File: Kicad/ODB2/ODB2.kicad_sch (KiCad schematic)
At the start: 32 parts, among them U1 STM32F412ZGTx

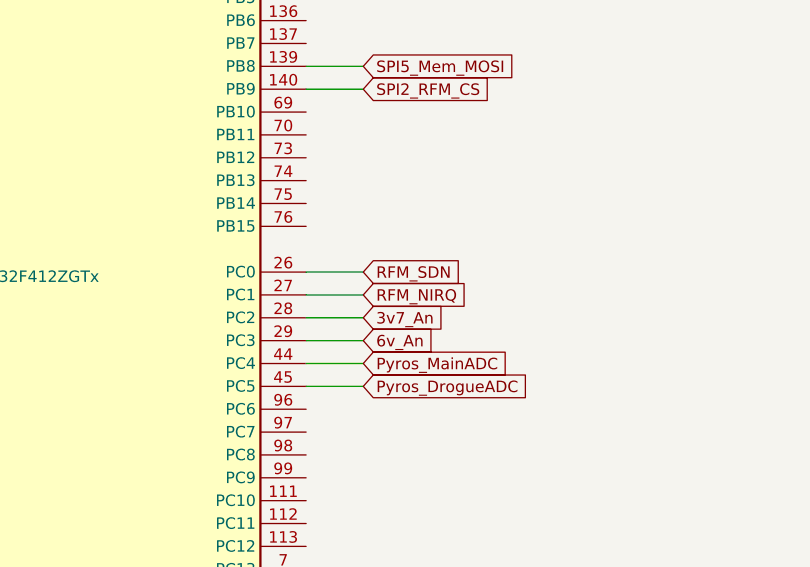
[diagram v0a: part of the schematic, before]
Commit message: Changed label 6v to 6v6 and changed circuit for the 6v6 batt led
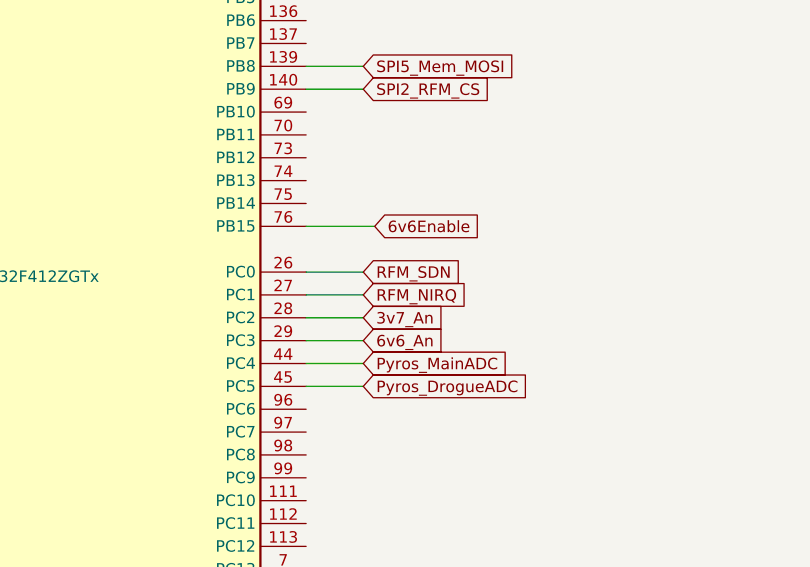
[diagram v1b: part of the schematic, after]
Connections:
- net 6v6Enable: now reaches U1.76 (PB15)
- net 6v_An renamed 6v6_An
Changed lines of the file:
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@@
+	(wire
+		(pts
+			(xy 231.14 137.16) (xy 238.76 137.16)
+		)
+		(stroke
+			(width 0)
+			(type default)
+		)
+	)
 	(wire
 		(pts
@@
 		)
 	)
+	(global_label "6v6Enable"
+		(shape input)
+		(at 238.76 137.16 0)
+		(fields_autoplaced yes)
+		(effects
+			(font
+				(size 1.27 1.27)
+			)
+			(justify left)
+		)
+		(property "Intersheetrefs" "${INTERSHEET_REFS}"
+			(at 251.4816 137.16 0)
+			(effects
+				(font
+					(size 1.27 1.27)
+				)
+				(justify left)
+				(hide yes)
+			)
+		)
+	)
 	(global_label "SPI5_Mem_MISO"
 		(shape input)
@@
 		)
 	)
-	(global_label "6v_An"
+	(global_label "6v6_An"
 		(shape input)
 		(at 237.49 149.86 0)
@@
 		)
 		(property "Intersheetrefs" "${INTERSHEET_REFS}"
-			(at 245.8575 149.86 0)
-			(effects
-				(font
+			(at 247.067 149.86 0)
+			(effects
+				(font

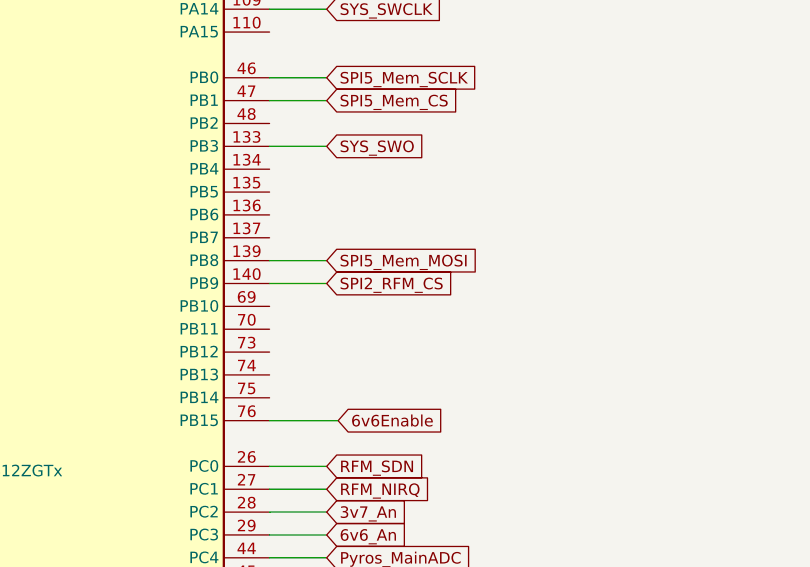
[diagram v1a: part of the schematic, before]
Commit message: fix spi label
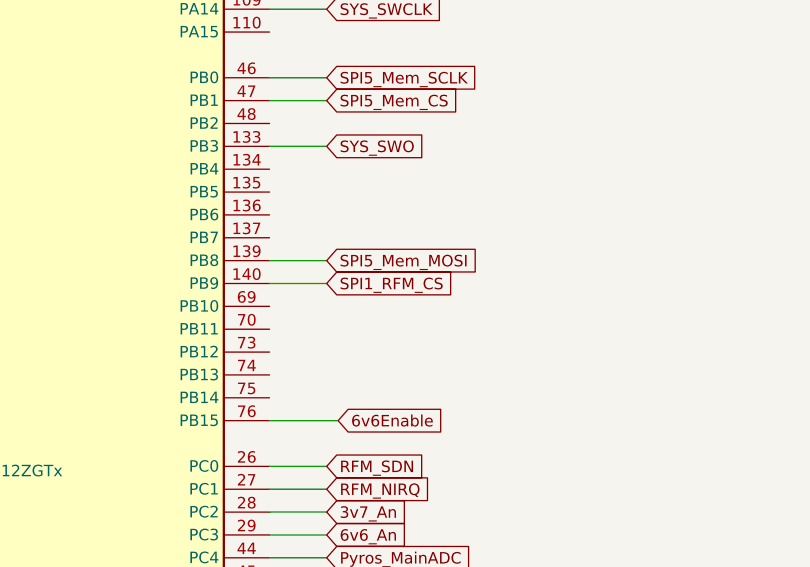
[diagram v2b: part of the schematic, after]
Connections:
- net SPI2_RFM_CS renamed SPI1_RFM_CS
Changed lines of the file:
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@@
 		)
 	)
-	(global_label "SPI2_RFM_CS"
+	(global_label "SPI1_RFM_CS"
 		(shape input)
 		(at 237.49 121.92 0)

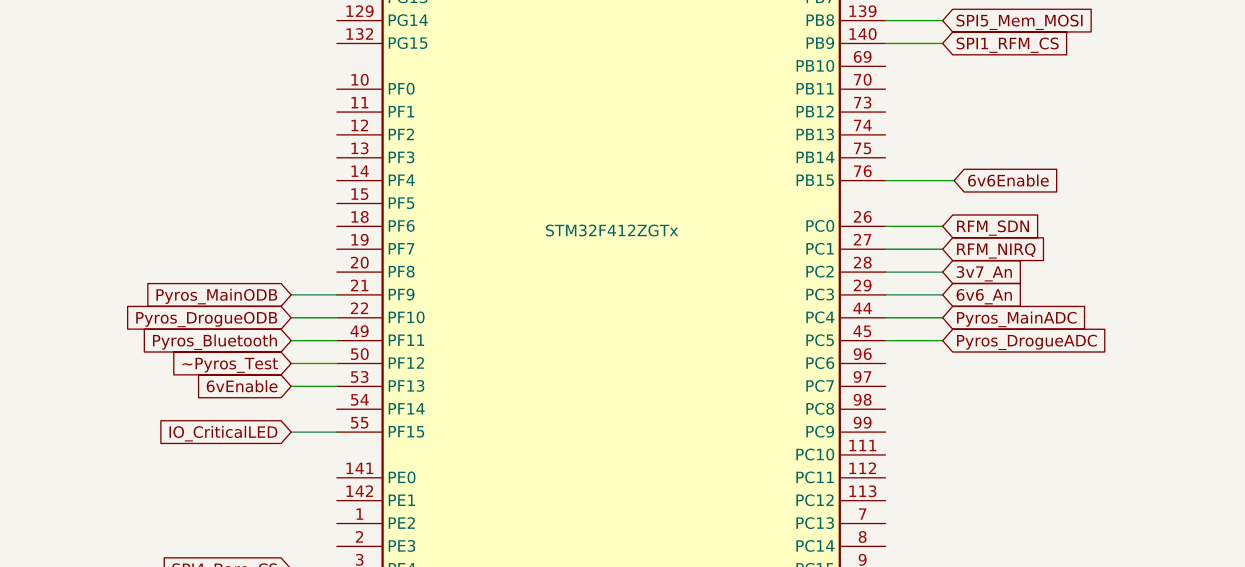
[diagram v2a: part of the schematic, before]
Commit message: fix 6v6Enable label
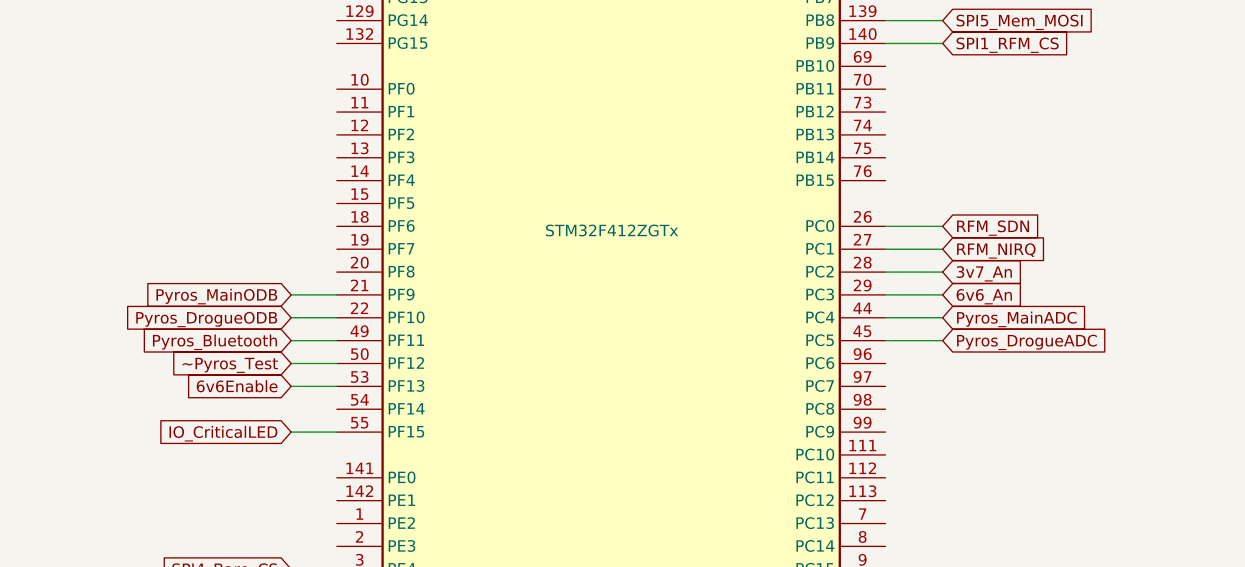
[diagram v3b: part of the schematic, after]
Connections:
- net 6vEnable is gone; now on net 6v6Enable: U1.53 (PF13)
- net 6v6Enable: no longer U1.76 (PB15)
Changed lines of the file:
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@@
-	(wire
-		(pts
-			(xy 231.14 137.16) (xy 238.76 137.16)
-		)
-		(stroke
-			(width 0)
-			(type default)
-		)
-	)
 	(wire
 		(pts
@@
 		)
 	)
-	(global_label "6vEnable"
+	(global_label "6v6Enable"
 		(shape input)
 		(at 165.1 160.02 180)
@@
 		)
 		(property "Intersheetrefs" "${INTERSHEET_REFS}"
-			(at 153.5879 160.02 0)
+			(at 152.3784 160.02 0)
 			(effects
 				(font
@@
 				(hide yes)
 			)
-		)
-	)
-	(global_label "6v6Enable"
-		(shape input)
-		(at 238.76 137.16 0)
-		(fields_autoplaced yes)
-		(effects
-			(font
-				(size 1.27 1.27)
-			)
-			(justify left)
-		)
-		(property "Intersheetrefs" "${INTERSHEET_REFS}"
-			(at 251.4816 137.16 0)
-			(effects
-				(font
-					(size 1.27 1.27)
-				)
-				(justify left)
-				(hide yes)
-			)

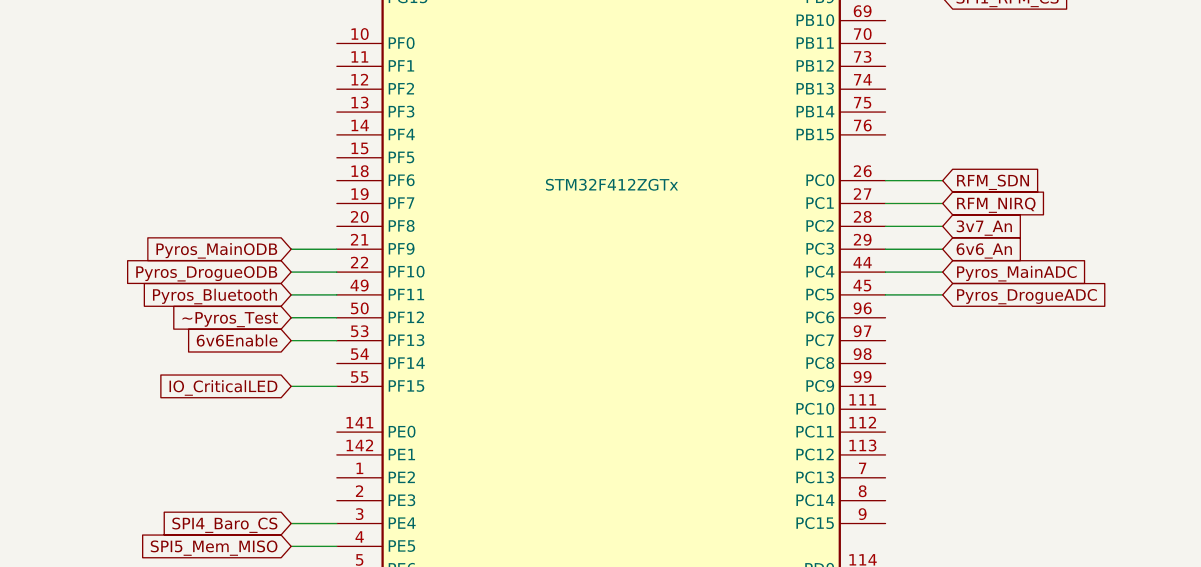
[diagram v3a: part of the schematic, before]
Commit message: changer LiFePO4 pour LiPo
recalculer le bon ration pour l'ADC du 4v2 input (anciennement 3v7 input) et modifier ces labels associées

modifier le bon ration (je crois) pour l'ADC du 7v4 isolation (anciennement 6v isolation) et modifier ces labels associées
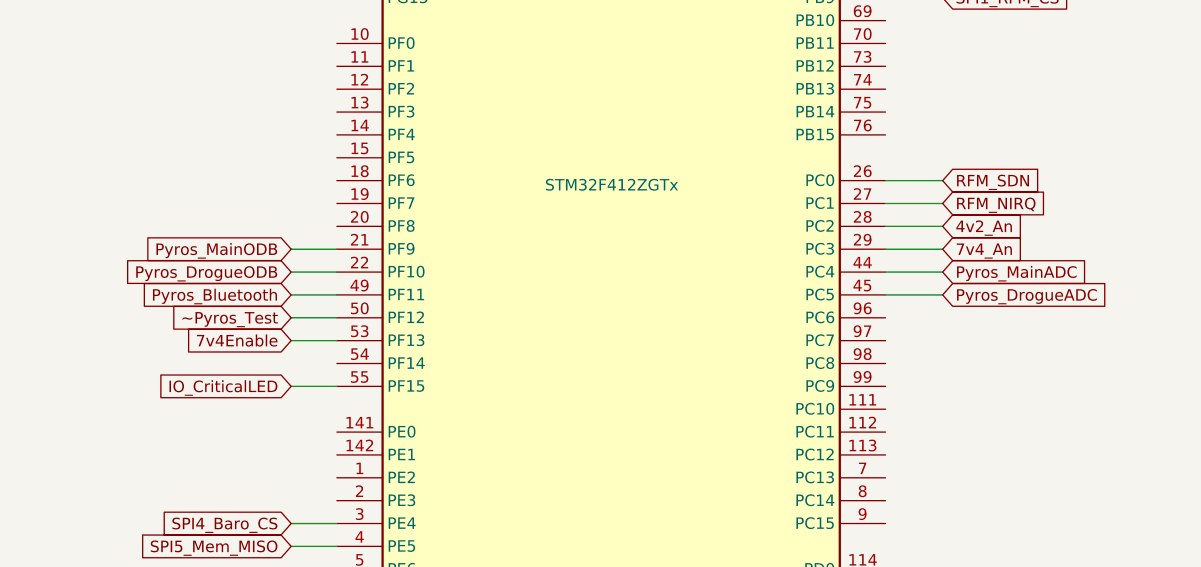
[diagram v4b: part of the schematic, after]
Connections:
- net 3v7_An renamed 4v2_An
- net 6v6Enable renamed 7v4Enable
- net 6v6_An renamed 7v4_An
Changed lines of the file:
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@@
 		)
 	)
-	(global_label "6v6Enable"
+	(global_label "7v4Enable"
 		(shape input)
 		(at 165.1 160.02 180)
@@
 		)
 	)
+	(global_label "4v2_An"
+		(shape input)
+		(at 237.49 147.32 0)
+		(fields_autoplaced yes)
+		(effects
+			(font
+				(size 1.27 1.27)
+			)
+			(justify left)
+		)
+		(property "Intersheetrefs" "${INTERSHEET_REFS}"
+			(at 247.067 147.32 0)
+			(effects
+				(font
+					(size 1.27 1.27)
+				)
+				(justify left)
+				(hide yes)
+			)
+		)
+	)
 	(global_label "SPI1_ICM_RFM_MOSI"
 		(shape input)
@@
 		)
 	)
-	(global_label "3v7_An"
-		(shape input)
-		(at 237.49 147.32 0)
-		(fields_autoplaced yes)
-		(effects
-			(font
-				(size 1.27 1.27)
-			)
-			(justify left)
-		)
-		(property "Intersheetrefs" "${INTERSHEET_REFS}"
-			(at 247.067 147.32 0)
-			(effects
-				(font
-					(size 1.27 1.27)
-				)
-				(justify left)
-				(hide yes)
-			)
-		)
-	)
 	(global_label "SPI1_ICM_CS"
 		(shape input)
@@
 		)
 	)
-	(global_label "6v6_An"
+	(global_label "7v4_An"
 		(shape input)
 		(at 237.49 149.86 0)

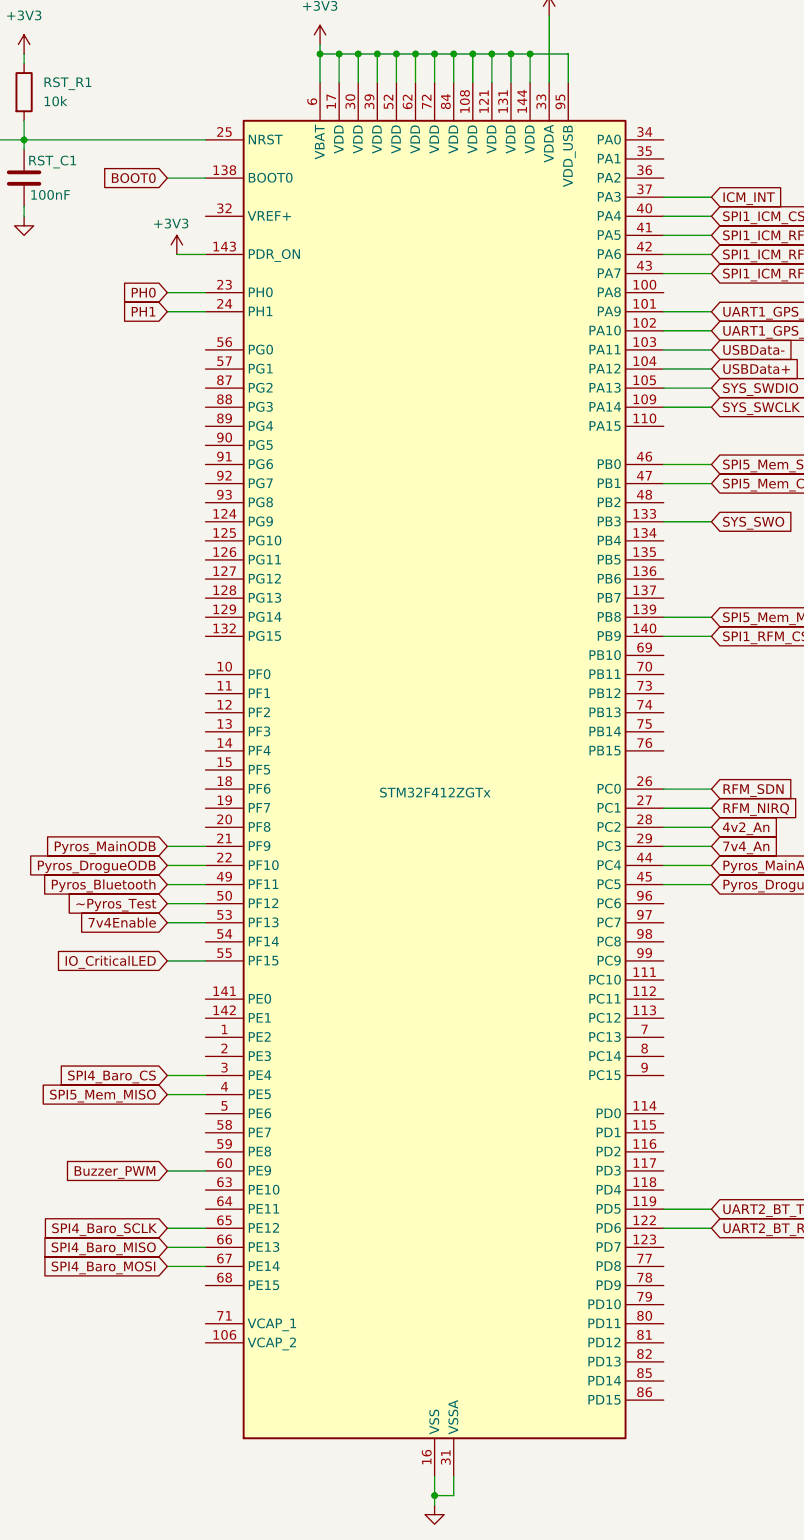
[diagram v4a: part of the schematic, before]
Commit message: Fix labels, 50 ohms, STM no connect
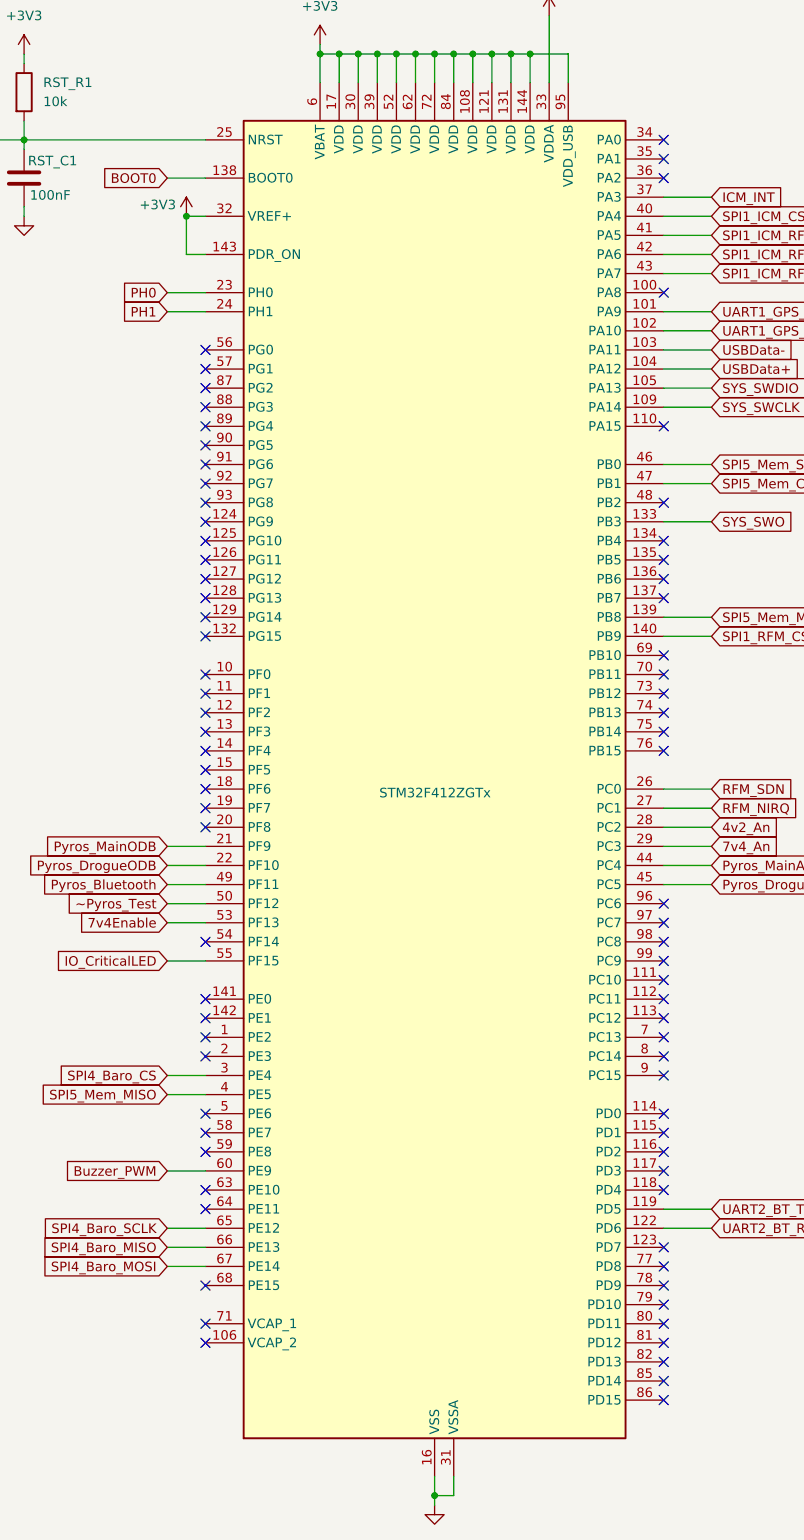
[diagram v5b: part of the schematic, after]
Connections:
- net +3V3: now also U1.32 (VREF+)
- no-connect marks 0 -> 78

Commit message: Final fixes
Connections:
- net 4v2_An renamed 3v7_An
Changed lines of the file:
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@@
+	(wire
+		(pts
+			(xy 167.64 64.77) (xy 167.64 66.04)
+		)
+		(stroke
+			(width 0)
+			(type default)
+		)
+	)
 	(wire
 		(pts
@@
 		)
 	)
-	(global_label "4v2_An"
+	(global_label "3v7_An"
 		(shape input)
 		(at 237.49 147.32 0)
@@
 	(symbol
 		(lib_id "power:+3V3")
-		(at 167.64 66.04 0)
+		(at 167.64 64.77 0)
 		(unit 1)
 		(exclude_from_sim no)
@@
 		(dnp no)
 		(property "Reference" "#PWR089"
-			(at 167.64 69.85 0)
+			(at 167.64 68.58 0)
 			(effects
 				(font
@@
 		)
 		(property "Value" "+3V3"
-			(at 163.83 64.516 0)
+			(at 164.084 65.786 0)
 			(effects
 				(font
@@
 		)
 		(property "Footprint" ""
-			(at 167.64 66.04 0)
+			(at 167.64 64.77 0)
 			(effects
 				(font
@@
 		)
 		(property "Datasheet" ""
-			(at 167.64 66.04 0)
+			(at 167.64 64.77 0)
 			(effects
 				(font
@@
 		)
 		(property "Description" "Power symbol creates a global label with name \"+3V3\""
-			(at 167.64 66.04 0)
-			(effects
-				(font
+			(at 167.64 64.77 0)
+			(effects
+				(font

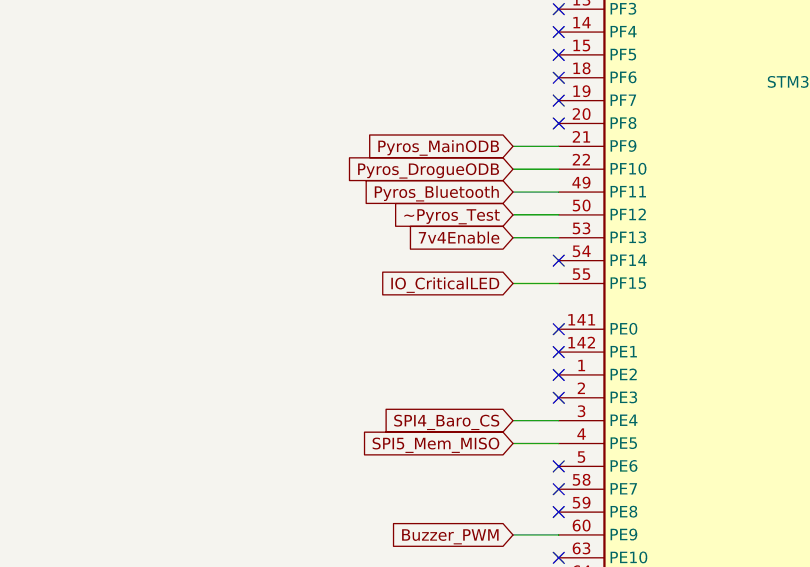
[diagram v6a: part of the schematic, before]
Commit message: fix Labels + fix STM32 projet pinout
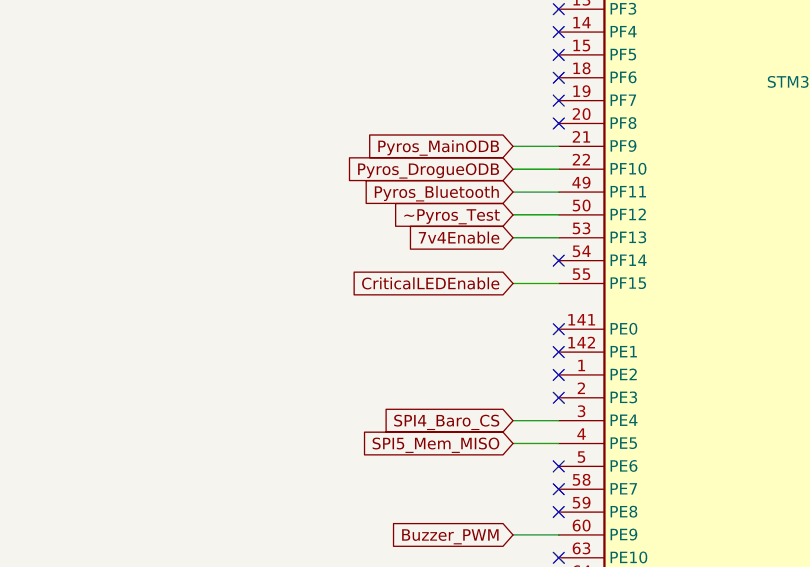
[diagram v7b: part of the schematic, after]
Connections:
- net IO_CriticalLED renamed CriticalLEDEnable
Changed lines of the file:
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@@
 		)
 	)
-	(global_label "IO_CriticalLED"
+	(global_label "CriticalLEDEnable"
 		(shape input)
 		(at 165.1 165.1 180)
@@
 		)
 		(property "Intersheetrefs" "${INTERSHEET_REFS}"
-			(at 148.8705 165.1 0)
+			(at 145.4236 165.1 0)
 			(effects
 				(font

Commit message: Minor fix et début layout STM et sensors
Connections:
- net GND: no longer Crystal_C2.1, Crystal_R1.2, Crystal_Y1.4
- new net: Crystal_C2.1, Crystal_R1.2, Crystal_Y1.4
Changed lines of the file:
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@@
-	)
-	(junction
-		(at 382.27 134.62)
-		(diameter 0)
-		(color 0 0 0 0)
 	)
 	(junction
@@
 	(wire
 		(pts
-			(xy 387.35 134.62) (xy 382.27 134.62)
-		)
-		(stroke
-			(width 0)
-			(type default)
-		)
-	)
-	(wire
-		(pts
 			(xy 165.1 160.02) (xy 170.18 160.02)
 		)
@@
 	(wire
 		(pts
-			(xy 382.27 127) (xy 382.27 134.62)
+			(xy 382.27 127) (xy 382.27 142.24)
 		)
 		(stroke
@@
 	(wire
 		(pts
-			(xy 379.73 134.62) (xy 382.27 134.62)
+			(xy 379.73 134.62) (xy 387.35 134.62)
 		)
 		(stroke
@@
 		)
 		(stroke
-			(width 0)
-			(type default)
-		)
-	)
-	(wire
-		(pts
-			(xy 382.27 134.62) (xy 382.27 142.24)
-		)
-		(stroke
